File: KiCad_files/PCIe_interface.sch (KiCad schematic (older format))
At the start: 13 parts, among them J1 PCIe_x4_Connector

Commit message: Cleanup for demo/presentation
Merged Config and Debug sheets.
Added GPIO for remaining pins.
Annotations.
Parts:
- gave numbers to parts that had none: 1
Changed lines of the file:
@@
 Connection ~ 5350 2200
 $Comp
-L GND #PWR01
+L GND #PWR1
 U 1 1 5BFDC477
 P 2950 5400
-F 0 "#PWR01" H 2950 5150 50  0001 C CNN
+F 0 "#PWR1" H 2950 5150 50  0001 C CNN
 F 1 "GND" H 2950 5250 50  0000 C CNN
 F 2 "" H 2950 5400 50  0001 C CNN
@@
 	5350 2400 5350 5400
 $Comp
-L GND #PWR02
+L GND #PWR2
 U 1 1 5BFDC630
 P 5350 5400
-F 0 "#PWR02" H 5350 5150 50  0001 C CNN
+F 0 "#PWR2" H 5350 5150 50  0001 C CNN
 F 1 "GND" H 5350 5250 50  0000 C CNN
 F 2 "" H 5350 5400 50  0001 C CNN
@@
 	8600 4500 8500 4500
 $Comp
-L XC7A35T_CSG325 U?
+L XC7A35T_CSG325 U1
 U 5 1 5C173C24
 P 7900 4500
-F 0 "U?" H 7900 4200 60  0000 C CNN
+F 0 "U1" H 7900 4200 60  0000 C CNN
 F 1 "XC7A35T_CSG325" H 7900 4300 60  0000 C CNN
 F 2 "" H 8200 6250 60  0001 C CNN

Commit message: Cleanup + Update to KiCad 5.0 + DDR2
Updated to KiCad 5, which re-organized libraries, so corrected them to not need RASAC-rescue.lib.
Also cleaned up some stuff.
DDR4 has been removed and in place will be DDR2.
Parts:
- C1, C10, C2, C3, C4, C5, C6, C7, C8, C9: symbol C_Small -> Device:C_Small
- J1: symbol PCIe_x4_Connector -> custom:PCIe_x4_Connector
- R1: symbol R -> Device:R
- U1: symbol XC7A35T_CSG325 -> custom:XC7A35T_CSG325
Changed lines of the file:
@@
-EESchema Schematic File Version 2
-LIBS:power
-LIBS:device
-LIBS:switches
-LIBS:relays
-LIBS:motors
-LIBS:transistors
-LIBS:conn
-LIBS:linear
-LIBS:regul
-LIBS:74xx
-LIBS:cmos4000
-LIBS:adc-dac
-LIBS:memory
-LIBS:xilinx
-LIBS:microcontrollers
-LIBS:dsp
-LIBS:microchip
-LIBS:analog_switches
-LIBS:motorola
-LIBS:texas
-LIBS:intel
-LIBS:audio
-LIBS:interface
-LIBS:digital-audio
-LIBS:philips
-LIBS:display
-LIBS:cypress
-LIBS:siliconi
-LIBS:opto
-LIBS:atmel
-LIBS:contrib
-LIBS:valves
-LIBS:custom
-LIBS:Connector
+EESchema Schematic File Version 4
 LIBS:RASAC-cache
-EELAYER 25 0
+EELAYER 26 0
 EELAYER END
 $Descr A4 11693 8268
@@
 $EndDescr
 $Comp
-L PCIe_x4_Connector J1
+L custom:PCIe_x4_Connector J1
 U 1 1 5BFDC341
 P 4150 3800
@@
 Connection ~ 5350 2200
 $Comp
-L GND #PWR1
+L power:GND #PWR01
 U 1 1 5BFDC477
 P 2950 5400
-F 0 "#PWR1" H 2950 5150 50  0001 C CNN
+F 0 "#PWR01" H 2950 5150 50  0001 C CNN
 F 1 "GND" H 2950 5250 50  0000 C CNN
 F 2 "" H 2950 5400 50  0001 C CNN
@@
 	5350 2400 5350 5400
 $Comp
-L GND #PWR2
+L power:GND #PWR02
 U 1 1 5BFDC630
 P 5350 5400
-F 0 "#PWR2" H 5350 5150 50  0001 C CNN
+F 0 "#PWR02" H 5350 5150 50  0001 C CNN
 F 1 "GND" H 5350 5250 50  0000 C CNN
 F 2 "" H 5350 5400 50  0001 C CNN
@@
 	3050 3600 2850 3600
 $Comp
-L C_Small C1
+L Device:C_Small C1
 U 1 1 5BFDCD53
 P 5750 3450
@@
 $EndComp
 $Comp
-L C_Small C2
+L Device:C_Small C2
 U 1 1 5BFDCDA6
 P 5750 3650
@@
 	5900 3500 6250 3500
 $Comp
-L C_Small C3
+L Device:C_Small C3
 U 1 1 5BFDD468
 P 6100 3750
@@
 $EndComp
 $Comp
-L C_Small C4
+L Device:C_Small C4
 U 1 1 5BFDD46E
 P 6100 3950
@@
 	5250 3800 5950 3800
 $Comp
-L C_Small C5
+L Device:C_Small C5
 U 1 1 5BFDE1F5
 P 6100 4250
@@
 $EndComp
 $Comp
-L C_Small C6
+L Device:C_Small C6
 U 1 1 5BFDE1FB
 P 6100 4450
@@
 	5250 4300 5950 4300
 $Comp
-L C_Small C7
+L Device:C_Small C7
 U 1 1 5BFDE267
 P 6100 4650
@@
 $EndComp
 $Comp
-L C_Small C8
+L Device:C_Small C8
 U 1 1 5BFDE26D
 P 6100 4850
@@
 	5250 4700 5950 4700
 $Comp
-L C_Small C9
+L Device:C_Small C9
 U 1 1 5BFDE2C1
 P 6100 5050
@@
 $EndComp
 $Comp
-L C_Small C10
+L Device:C_Small C10
 U 1 1 5BFDE2C7
 P 6100 5250
@@
 MGTAVTT
 $Comp
-L R R1
+L Device:R R1
 U 1 1 5C0632A0
 P 8650 2500
@@
 	8600 4500 8500 4500
 $Comp
-L XC7A35T_CSG325 U1
+L custom:XC7A35T_CSG325 U1
 U 5 1 5C173C24
 P 7900 4500

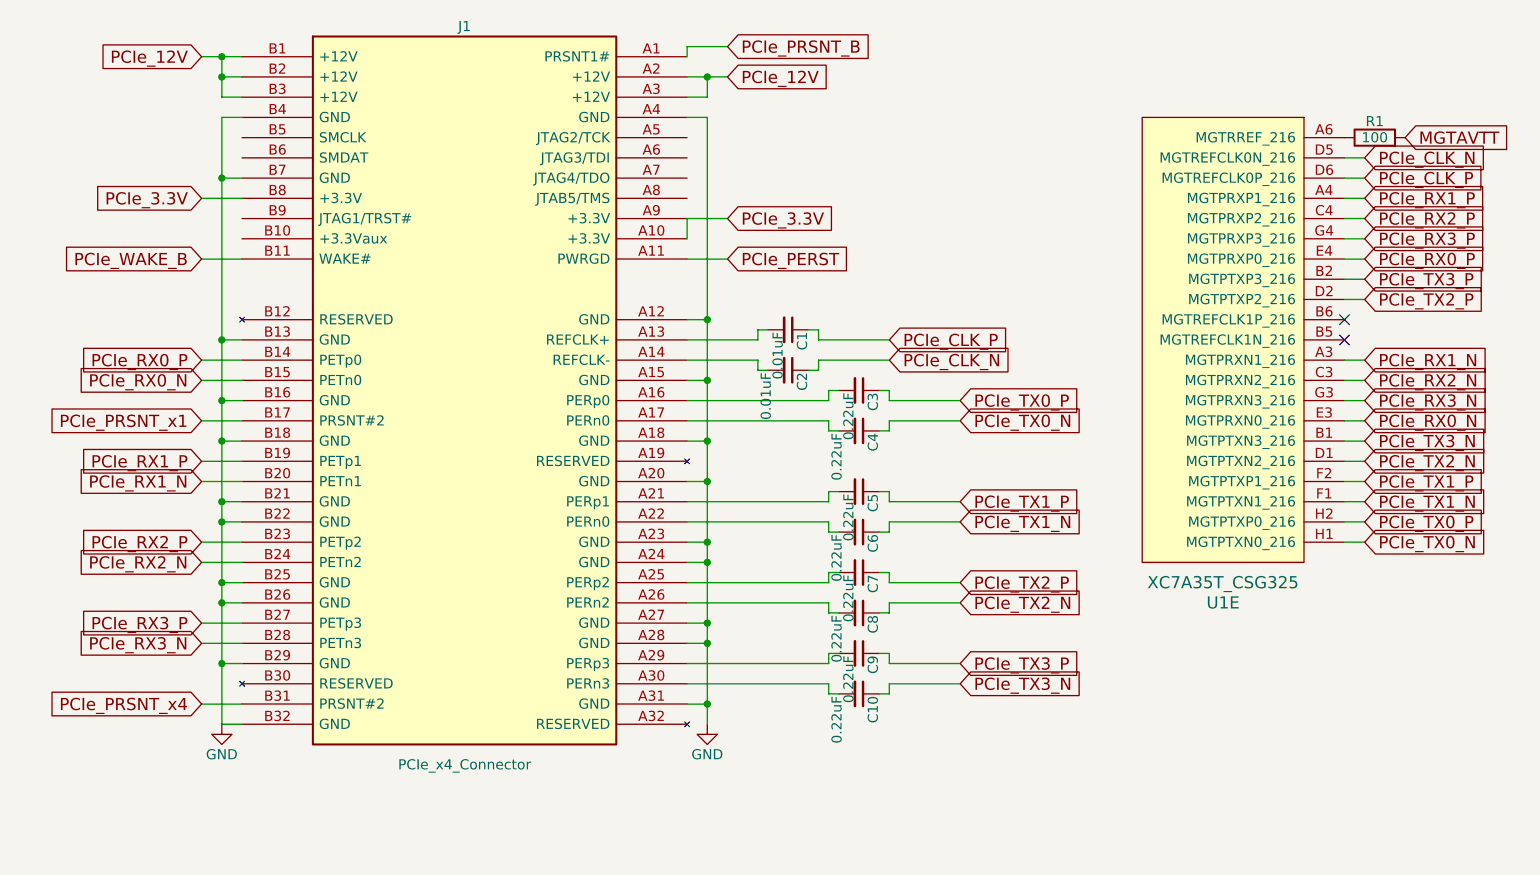
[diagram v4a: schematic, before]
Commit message: Minor fixes
Still fixing from KiCad update
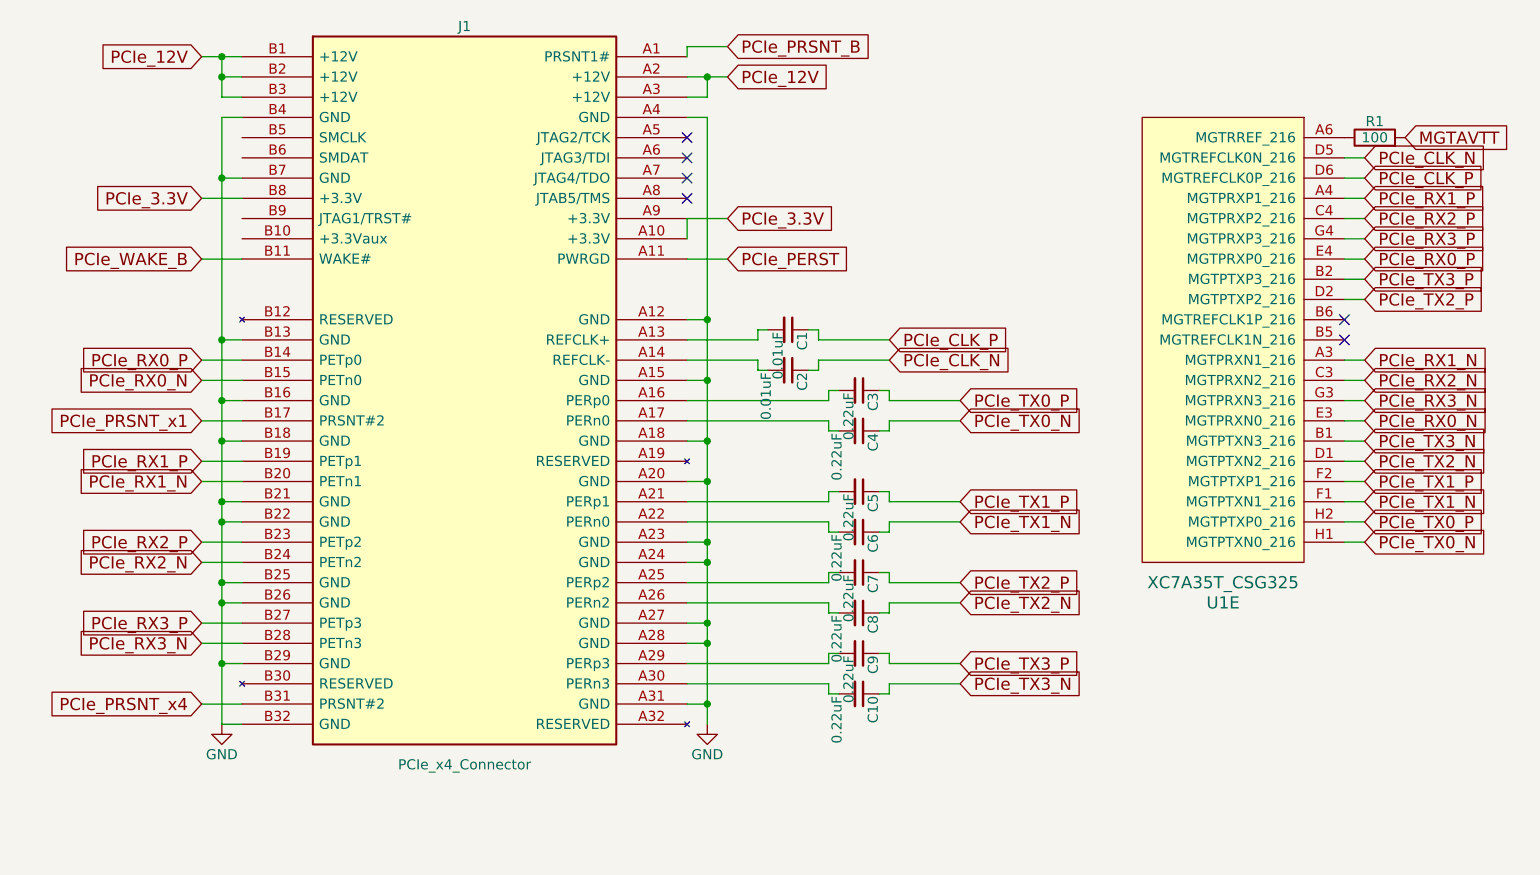
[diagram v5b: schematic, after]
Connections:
- no-connect marks 2 -> 6
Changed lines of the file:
@@
 	2950 2300 3050 2300
 Wire Wire Line
-	2950 2100 2950 2300
-Wire Wire Line
-	2850 2100 3050 2100
+	2950 2100 2950 2200
+Wire Wire Line
+	2850 2100 2950 2100
 Connection ~ 2950 2100
 Wire Wire Line
@@
 Connection ~ 2950 2200
 Wire Wire Line
-	5250 2200 5450 2200
+	5250 2200 5350 2200
 Wire Wire Line
 	5350 2200 5350 2300
@@
 	3050 2400 2950 2400
 Wire Wire Line
-	2950 2400 2950 5400
+	2950 2400 2950 2700
 Wire Wire Line
 	2950 5400 3050 5400
@@
 	5350 5300 5250 5300
 Wire Wire Line
-	5350 2400 5350 5400
+	5350 2400 5350 3400
 $Comp
 L power:GND #PWR02
@@
 	1    0    0    -1
 $EndComp
+Wire Wire Line
+	2950 2100 3050 2100
+Wire Wire Line
+	2950 2200 2950 2300
+Wire Wire Line
+	5350 2200 5450 2200
+Wire Wire Line
+	2950 2700 2950 3500
+Wire Wire Line
+	2950 3500 2950 3800
+Wire Wire Line
+	2950 3800 2950 4000
+Wire Wire Line
+	2950 4000 2950 4300
+Wire Wire Line
+	2950 4300 2950 4400
+Wire Wire Line
+	2950 4400 2950 4700
+Wire Wire Line
+	2950 4700 2950 4800
+Wire Wire Line
+	2950 4800 2950 5100
+Wire Wire Line
+	2950 5100 2950 5400
+Wire Wire Line
+	5350 5300 5350 5400
+Wire Wire Line
+	5350 3400 5350 3700
+Wire Wire Line
+	5350 3700 5350 4000
+Wire Wire Line
+	5350 4000 5350 4200
+Wire Wire Line
+	5350 4200 5350 4500
+Wire Wire Line
+	5350 4500 5350 4600
+Wire Wire Line
+	5350 4600 5350 4900
+Wire Wire Line
+	5350 4900 5350 5000
+Wire Wire Line
+	5350 5000 5350 5300
+NoConn ~ 5250 2500
+NoConn ~ 5250 2600
+NoConn ~ 5250 2700
+NoConn ~ 5250 2800
 $EndSCHEMATC

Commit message: Config_Debug and PCIe sheets look done
Added jumpers to JTAG chain.
Placed NCs on not used pins.
PCIe_PRSNT_B should be connected to the furthest PCIe_PRSNT_#.
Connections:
- net PCIe_PRSNT_x4 is gone; now on net PCIe_PRSNT_B: J1.B31 (PRSNT#2)
- net PCIe_PRSNT_x1: no longer names the net of J1.B17 (PRSNT#2)
- no-connect marks 6 -> 11
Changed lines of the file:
@@
 Wire Wire Line
 	5250 2050 5450 2050
-Text GLabel 2850 3900 0    60   Input ~ 0
-PCIe_PRSNT_x1
 Wire Wire Line
 	2850 3900 3050 3900
@@
 NoConn ~ 5250 2700
 NoConn ~ 5250 2800
+Connection ~ 5250 2900
+NoConn ~ 3050 2500
+NoConn ~ 3050 2600
+NoConn ~ 3050 2900
+NoConn ~ 3050 3000
+NoConn ~ 2850 3900
+Text GLabel 3800 6000 0    60   Input ~ 0
+PCIe_PRSNT_B
+Text GLabel 4300 6000 2    60   Input ~ 0
+PCIe_PRSNT_x4
+Wire Wire Line
+	4300 6000 3800 6000
 $EndSCHEMATC

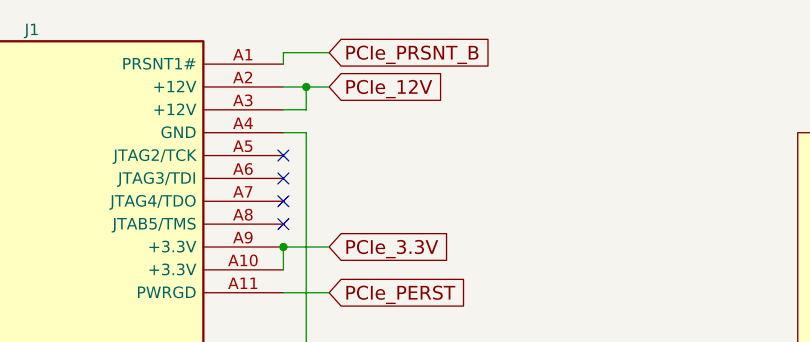
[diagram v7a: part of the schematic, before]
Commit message: Cleanup for DRC and HDMI. HDMI and DDR2 looks good
DRC returns 5 errors with POWEROUTPUT-POWEROUTPUT set as good.
3 of them come from 3V3 since it's being driven from a MOSFET.
1 of them from VCC5V0 not yet supplied.
1 of them from USB_VBUS not set as output.
TODO:
5V supply for HDMI
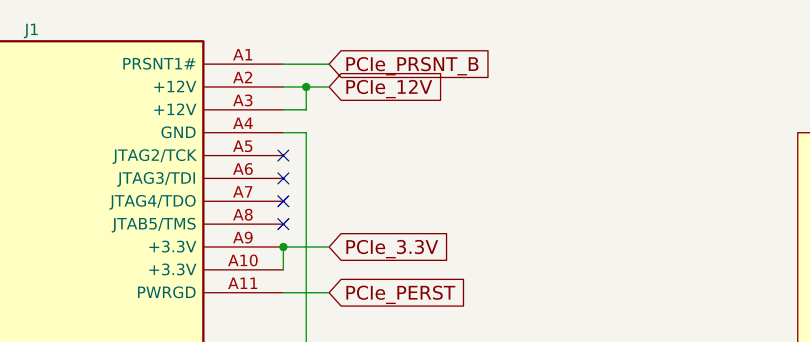
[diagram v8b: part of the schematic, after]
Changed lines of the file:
@@
 	5250 5000 5350 5000
 Connection ~ 5350 5000
-Text GLabel 5450 2050 2    60   Input ~ 0
+Text GLabel 5450 2100 2    60   Input ~ 0
 PCIe_PRSNT_B
 Wire Wire Line
-	5250 2100 5250 2050
-Wire Wire Line
-	5250 2050 5450 2050
+	5250 2100 5450 2100
 Wire Wire Line
 	2850 3900 3050 3900
@@
 U 5 1 5C173C24
 P 7900 4500
+AR Path="/5C173C24" Ref="U1"  Part="5"
+AR Path="/5BFDC338/5C173C24" Ref="U1"  Part="5"
 F 0 "U1" H 7900 4200 60  0000 C CNN
 F 1 "XC7A35T_CSG325" H 7900 4300 60  0000 C CNN
